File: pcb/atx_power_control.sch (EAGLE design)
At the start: 57 parts, among them IC2 REG1117, IC3 STM32F042F4, IC4 MY_7905DT, J1 ATX24RH, SW1 324_SW, SW2 324_SW, SW3 324_SW, SW4 324_SW, U2 USBC_16P

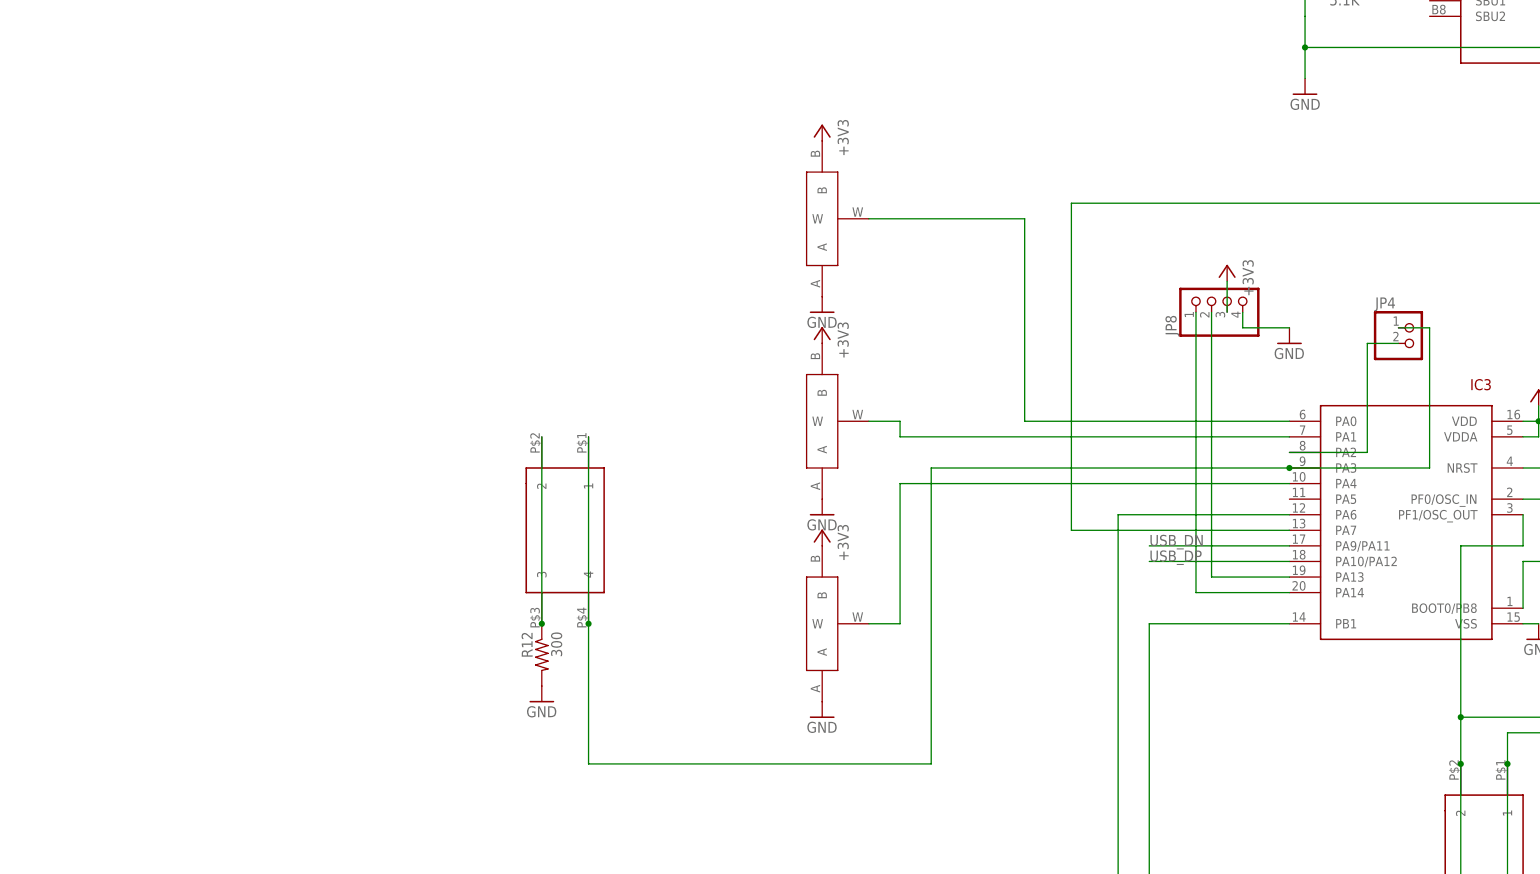
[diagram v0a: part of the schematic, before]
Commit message: removed pot and added buttons and header
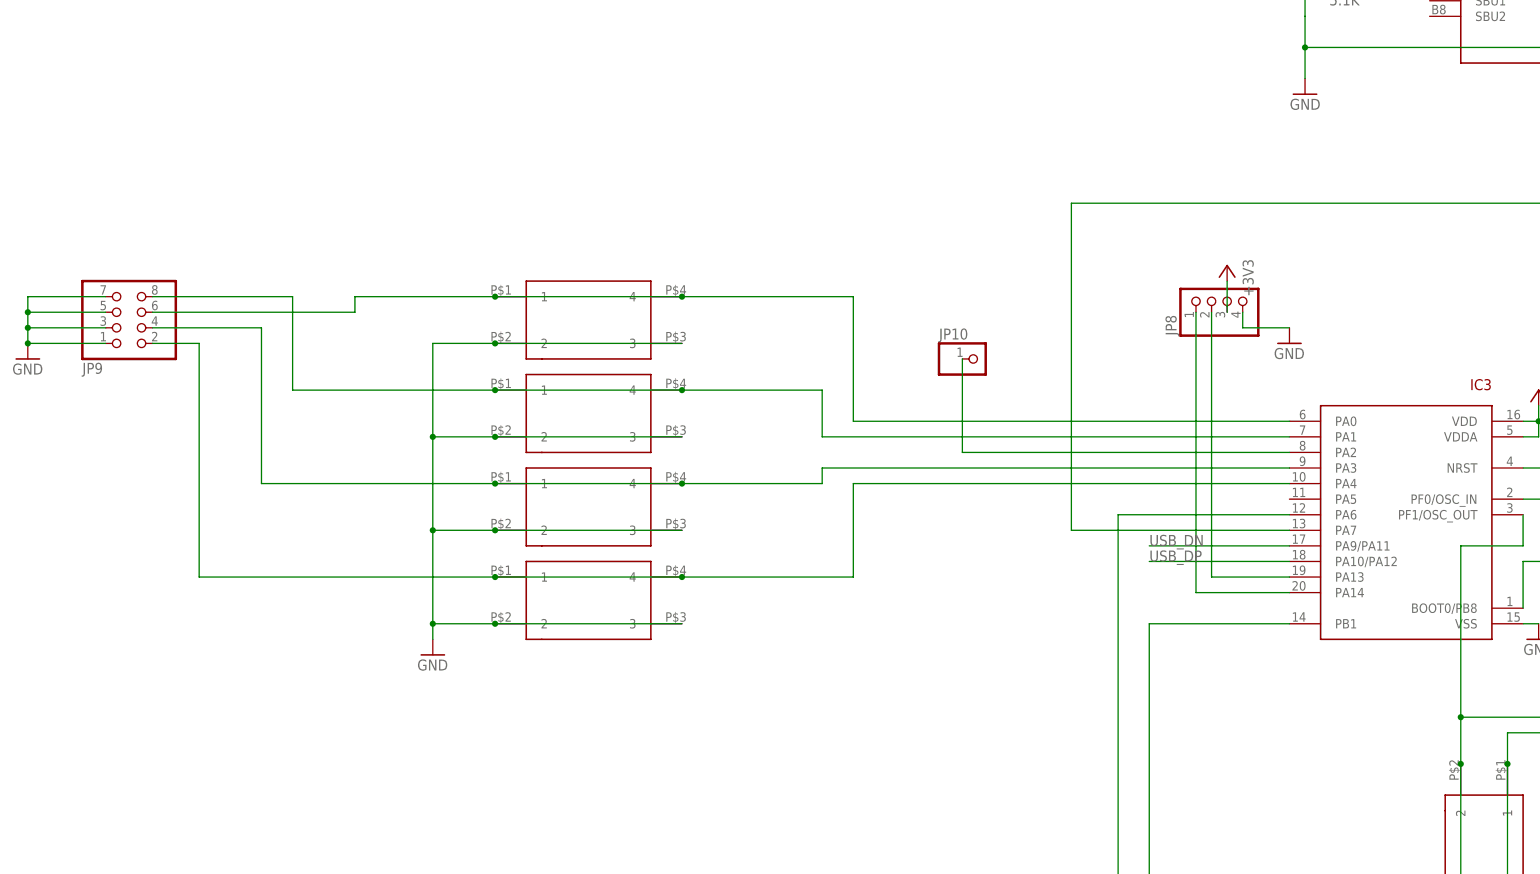
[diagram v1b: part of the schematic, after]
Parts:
- removed JP4: (no value), pinhead:PINHD-1X2
- removed R12: 300, joyAnalog:RESISTOR0805-RES
- removed U$4, U$5, U$6: 3386P, bbc_micro:3386P
- added JP10: (no value), adafruit_changed:PINHD-1X1
- added JP9: (no value), pinhead:PINHD-2X4
- added SW5, SW6, SW7: 324_SW, 3pos_slide_switch_centered:324_SW
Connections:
- removed net N$32: R12.1, SW2.2, SW2.3
- net +3V3: no longer U$4.B, U$5.B, U$6.B
- net GND: now also JP9.1, JP9.3, JP9.5, JP9.7, SW2.2, SW2.3, SW5.2, SW5.3, SW6.2, SW6.3, SW7.2, SW7.3; no longer R12.2, U$4.A, U$5.A, U$6.A
- net N$13: now also JP9.6, SW2.1, SW2.4; no longer U$4.W
- net N$22: now also JP9.8, SW5.1, SW5.4; no longer U$5.W
- net N$23: now also IC3.PA2, JP10.1; no longer IC3.PA4, U$6.W
- net N$27: now also IC3.PA4, JP9.2, SW7.1, SW7.4; no longer IC3.PA2, JP4.2
- net N$30: now also JP9.4, SW6.1, SW6.4; no longer JP4.1, SW2.1, SW2.4

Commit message: atx rgb done, updated atx psu board too
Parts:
- added R12, R13, R14: 5.1K, joyAnalog:RESISTOR0805-RES
- added U1: USBC_16P, my_usbc_16p:USBC_16P
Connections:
- removed net N$14: IC3.PA7, JP7.2
- new net N$32: R12.1, U1.CC2
- new net N$34: R13.1, U1.CC1
- new net N$35: IC3.PA7, JP7.2, U1.DP1, U1.DP2
- new net N$36: JP7.3, U1.DN1, U1.DN2
- net GND: now also R12.2, R13.2, U1.GND; no longer JP7.3
- net N$12: now also R14.1
- net N$15: now also U1.VBUS
- net USB_DN: now also R14.2
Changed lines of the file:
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@@
 <part name="JP9" library="pinhead" library_urn="urn:adsk.eagle:library:325" deviceset="PINHD-2X4" device="" package3d_urn="urn:adsk.eagle:package:22461/2"/>
 <part name="JP10" library="adafruit_changed" deviceset="PINHD-1X1" device=""/>
+<part name="U1" library="my_usbc_16p" deviceset="USBC_16P" device=""/>
+<part name="GND31" library="supply1" deviceset="GND" device=""/>
+<part name="R12" library="joyAnalog" deviceset="RESISTOR" device="0805-RES" value="5.1K"/>
+<part name="R13" library="joyAnalog" deviceset="RESISTOR" device="0805-RES" value="5.1K"/>
+<part name="R14" library="joyAnalog" deviceset="RESISTOR" device="0805-RES" value="5.1K"/>
 </parts>
 <sheets>
@@
 <attribute name="NAME" x="-74.93" y="53.975" size="1.778" layer="95"/>
 <attribute name="VALUE" x="-74.93" y="45.72" size="1.778" layer="96"/>
+</instance>
+<instance part="U1" gate="G$1" x="279.4" y="111.76" smashed="yes" rot="MR0"/>
+<instance part="GND31" gate="1" x="241.3" y="104.14" smashed="yes" rot="MR0">
+<attribute name="VALUE" x="243.84" y="101.6" size="1.778" layer="96" rot="MR0"/>
+</instance>
+<instance part="R12" gate="G$1" x="246.38" y="121.92" smashed="yes" rot="MR0">
+<attribute name="NAME" x="250.19" y="123.4186" size="1.778" layer="95" rot="MR0"/>
+<attribute name="VALUE" x="250.19" y="118.618" size="1.778" layer="96" rot="MR0"/>
+<attribute name="NAME" x="250.19" y="123.4186" size="1.778" layer="95" rot="MR0"/>
+<attribute name="VALUE" x="250.19" y="118.618" size="1.778" layer="96" rot="MR0"/>
+</instance>
+<instance part="R13" gate="G$1" x="246.38" y="127" smashed="yes" rot="MR0">
+<attribute name="NAME" x="250.19" y="128.4986" size="1.778" layer="95" rot="MR0"/>
+<attribute name="VALUE" x="250.19" y="123.698" size="1.778" layer="96" rot="MR0"/>
+<attribute name="NAME" x="250.19" y="128.4986" size="1.778" layer="95" rot="MR0"/>
+<attribute name="VALUE" x="250.19" y="123.698" size="1.778" layer="96" rot="MR0"/>
+</instance>
+<instance part="R14" gate="G$1" x="-71.12" y="71.12" smashed="yes" rot="MR270">
+<attribute name="NAME" x="-72.6186" y="74.93" size="1.778" layer="95" rot="MR270"/>
+<attribute name="VALUE" x="-67.818" y="74.93" size="1.778" layer="96" rot="MR270"/>
+<attribute name="NAME" x="-72.6186" y="74.93" size="1.778" layer="95" rot="MR270"/>
+<attribute name="VALUE" x="-67.818" y="74.93" size="1.778" layer="96" rot="MR270"/>
 </instance>
 </instances>
@@
 <pinref part="GND15" gate="1" pin="GND"/>
 <wire x1="299.72" y1="60.96" x2="289.56" y2="60.96" width="0.1524" layer="91"/>
-<pinref part="JP7" gate="A" pin="3"/>
-<wire x1="299.72" y1="63.5" x2="289.56" y2="63.5" width="0.1524" layer="91"/>
-<wire x1="289.56" y1="63.5" x2="289.56" y2="60.96" width="0.1524" layer="91"/>
-<junction x="289.56" y="60.96"/>
 </segment>
 <segment>
@@
 <pinref part="JP9" gate="A" pin="7"/>
 </segment>
+<segment>
+<pinref part="GND31" gate="1" pin="GND"/>
+<wire x1="241.3" y1="116.84" x2="241.3" y2="111.76" width="0.1524" layer="91"/>
+<pinref part="R12" gate="G$1" pin="2"/>
+<wire x1="241.3" y1="111.76" x2="241.3" y2="106.68" width="0.1524" layer="91"/>
+<wire x1="241.3" y1="121.92" x2="241.3" y2="116.84" width="0.1524" layer="91"/>
+<junction x="241.3" y="121.92"/>
+<pinref part="R13" gate="G$1" pin="2"/>
+<wire x1="241.3" y1="127" x2="241.3" y2="121.92" width="0.1524" layer="91"/>
+<wire x1="294.64" y1="111.76" x2="241.3" y2="111.76" width="0.1524" layer="91"/>
+<junction x="241.3" y="111.76"/>
+<pinref part="U1" gate="G$1" pin="GND"/>
+</segment>
 </net>
 <net name="+3V3" class="0">
@@
 <segment>
 <pinref part="IC3" gate="G$1" pin="PA9/PA11"/>
-<wire x1="-40.64" y1="20.32" x2="-17.78" y2="20.32" width="0.1524" layer="91"/>
+<wire x1="-60.96" y1="20.32" x2="-17.78" y2="20.32" width="0.1524" layer="91"/>
 <label x="-40.64" y="20.32" size="1.778" layer="95"/>
+<wire x1="-60.96" y1="20.32" x2="-60.96" y2="66.04" width="0.1524" layer="91"/>
+<pinref part="R14" gate="G$1" pin="2"/>
+<wire x1="-60.96" y1="66.04" x2="-71.12" y2="66.04" width="0.1524" layer="91"/>
 </segment>
 </net>
@@
 <junction x="251.46" y="22.86"/>
 <pinref part="F3" gate="G$1" pin="1"/>
+<wire x1="251.46" y1="22.86" x2="251.46" y2="81.28" width="0.1524" layer="91"/>
+<wire x1="251.46" y1="81.28" x2="-71.12" y2="81.28" width="0.1524" layer="91"/>
+<pinref part="R14" gate="G$1" pin="1"/>
+<wire x1="-71.12" y1="81.28" x2="-71.12" y2="76.2" width="0.1524" layer="91"/>
 </segment>
 </net>
@@
 <wire x1="307.34" y1="68.58" x2="307.34" y2="40.64" width="0.1524" layer="91"/>
 <junction x="307.34" y="40.64"/>
+<pinref part="U1" gate="G$1" pin="VBUS"/>
+<wire x1="307.34" y1="68.58" x2="307.34" y2="132.08" width="0.1524" layer="91"/>
+<wire x1="307.34" y1="132.08" x2="294.64" y2="132.08" width="0.1524" layer="91"/>
+<junction x="307.34" y="68.58"/>
 </segment>
 </net>
@@
 </segment>
 </net>
-<net name="N$14" class="0">
-<segment>
-<pinref part="JP7" gate="A" pin="2"/>
-<wire x1="299.72" y1="66.04" x2="111.76" y2="66.04" width="0.1524" layer="91"/>
-<wire x1="111.76" y1="66.04" x2="111.76" y2="76.2" width="0.1524" layer="91"/>
-<wire x1="111.76" y1="76.2" x2="-53.34" y2="76.2" width="0.1524" layer="91"/>
-<wire x1="-53.34" y1="76.2" x2="-53.34" y2="22.86" width="0.1524" layer="91"/>
-<pinref part="IC3" gate="G$1" pin="PA7"/>
-<wire x1="-53.34" y1="22.86" x2="-17.78" y2="22.86" width="0.1524" layer="91"/>
-</segment>
-</net>
 <net name="N$17" class="0">
 <segment>
@@
 </segment>
 </net>
+<net name="N$32" class="0">
+<segment>
+<pinref part="R12" gate="G$1" pin="1"/>
+<wire x1="254" y1="121.92" x2="251.46" y2="121.92" width="0.1524" layer="91"/>
+<wire x1="261.62" y1="124.46" x2="254" y2="124.46" width="0.1524" layer="91"/>
+<wire x1="254" y1="124.46" x2="254" y2="121.92" width="0.1524" layer="91"/>
+<pinref part="U1" gate="G$1" pin="CC2"/>
+</segment>
+</net>
+<net name="N$34" class="0">
+<segment>
+<pinref part="R13" gate="G$1" pin="1"/>
+<wire x1="261.62" y1="127" x2="251.46" y2="127" width="0.1524" layer="91"/>
+<pinref part="U1" gate="G$1" pin="CC1"/>
+</segment>
+</net>
+<net name="N$35" class="0">
+<segment>
+<pinref part="U1" gate="G$1" pin="DP1"/>
+<pinref part="U1" gate="G$1" pin="DP2"/>
+<wire x1="294.64" y1="127" x2="294.64" y2="124.46" width="0.1524" layer="91"/>
+<wire x1="294.64" y1="127" x2="302.26" y2="127" width="0.1524" layer="91"/>
+<wire x1="302.26" y1="127" x2="302.26" y2="83.82" width="0.1524" layer="91"/>
+<junction x="294.64" y="127"/>
+<pinref part="JP7" gate="A" pin="2"/>
+<wire x1="299.72" y1="66.04" x2="292.1" y2="66.04" width="0.1524" layer="91"/>
+<wire x1="292.1" y1="66.04" x2="111.76" y2="66.04" width="0.1524" layer="91"/>
+<wire x1="111.76" y1="66.04" x2="111.76" y2="76.2" width="0.1524" layer="91"/>
+<wire x1="111.76" y1="76.2" x2="-53.34" y2="76.2" width="0.1524" layer="91"/>
+<wire x1="-53.34" y1="76.2" x2="-53.34" y2="22.86" width="0.1524" layer="91"/>
+<pinref part="IC3" gate="G$1" pin="PA7"/>
+<wire x1="-53.34" y1="22.86" x2="-17.78" y2="22.86" width="0.1524" layer="91"/>
+<wire x1="302.26" y1="83.82" x2="292.1" y2="83.82" width="0.1524" layer="91"/>
+<wire x1="292.1" y1="83.82" x2="292.1" y2="66.04" width="0.1524" layer="91"/>
+<junction x="292.1" y="66.04"/>
+</segment>
+</net>
+<net name="N$36" class="0">
+<segment>
+<pinref part="U1" gate="G$1" pin="DN1"/>
+<pinref part="U1" gate="G$1" pin="DN2"/>
+<wire x1="294.64" y1="119.38" x2="294.64" y2="116.84" width="0.1524" layer="91"/>
+<wire x1="294.64" y1="116.84" x2="297.18" y2="116.84" width="0.1524" layer="91"/>
+<junction x="294.64" y="116.84"/>
+<wire x1="297.18" y1="116.84" x2="297.18" y2="86.36" width="0.1524" layer="91"/>
+<wire x1="297.18" y1="86.36" x2="289.56" y2="86.36" width="0.1524" layer="91"/>
+<wire x1="289.56" y1="86.36" x2="289.56" y2="63.5" width="0.1524" layer="91"/>
+<pinref part="JP7" gate="A" pin="3"/>
+<wire x1="289.56" y1="63.5" x2="299.72" y2="63.5" width="0.1524" layer="91"/>
+</segment>
+</net>
